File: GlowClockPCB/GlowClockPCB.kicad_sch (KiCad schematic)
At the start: 32 parts, among them J1 LED_OUT_1, J2 LED_OUT_2, J3 LED_OUT_3, J4 LED_OUT_4, J5 POWER_IN, U1 RaspberryPi_Pico_W, U2 Raspberry_Pi_Zero_2_W, U3 DS3231MZ

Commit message: add output connectors for motor drivers
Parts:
- added J6: Motor_1_Out, Connector_JST:JST_XH_B4B-XH-A_1x04_P2.50mm_Vertical, symbol Connector:Conn_01x04_Socket
- added J7: Motor_2_Out, Connector_JST:JST_XH_B4B-XH-A_1x04_P2.50mm_Vertical, symbol Connector:Conn_01x04_Socket
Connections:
- net at A1.3 (A2): now also J6.4 (Pin_4)
- net at A1.4 (A1): now also J6.3 (Pin_3)
- net at A1.5 (B1): now also J6.2 (Pin_2)
- net at A1.6 (B2): now also J6.1 (Pin_1)
- net at A2.3 (A2): now also J7.4 (Pin_4)
- net at A2.4 (A1): now also J7.3 (Pin_3)
- net at A2.5 (B1): now also J7.2 (Pin_2)
- net at A2.6 (B2): now also J7.1 (Pin_1)

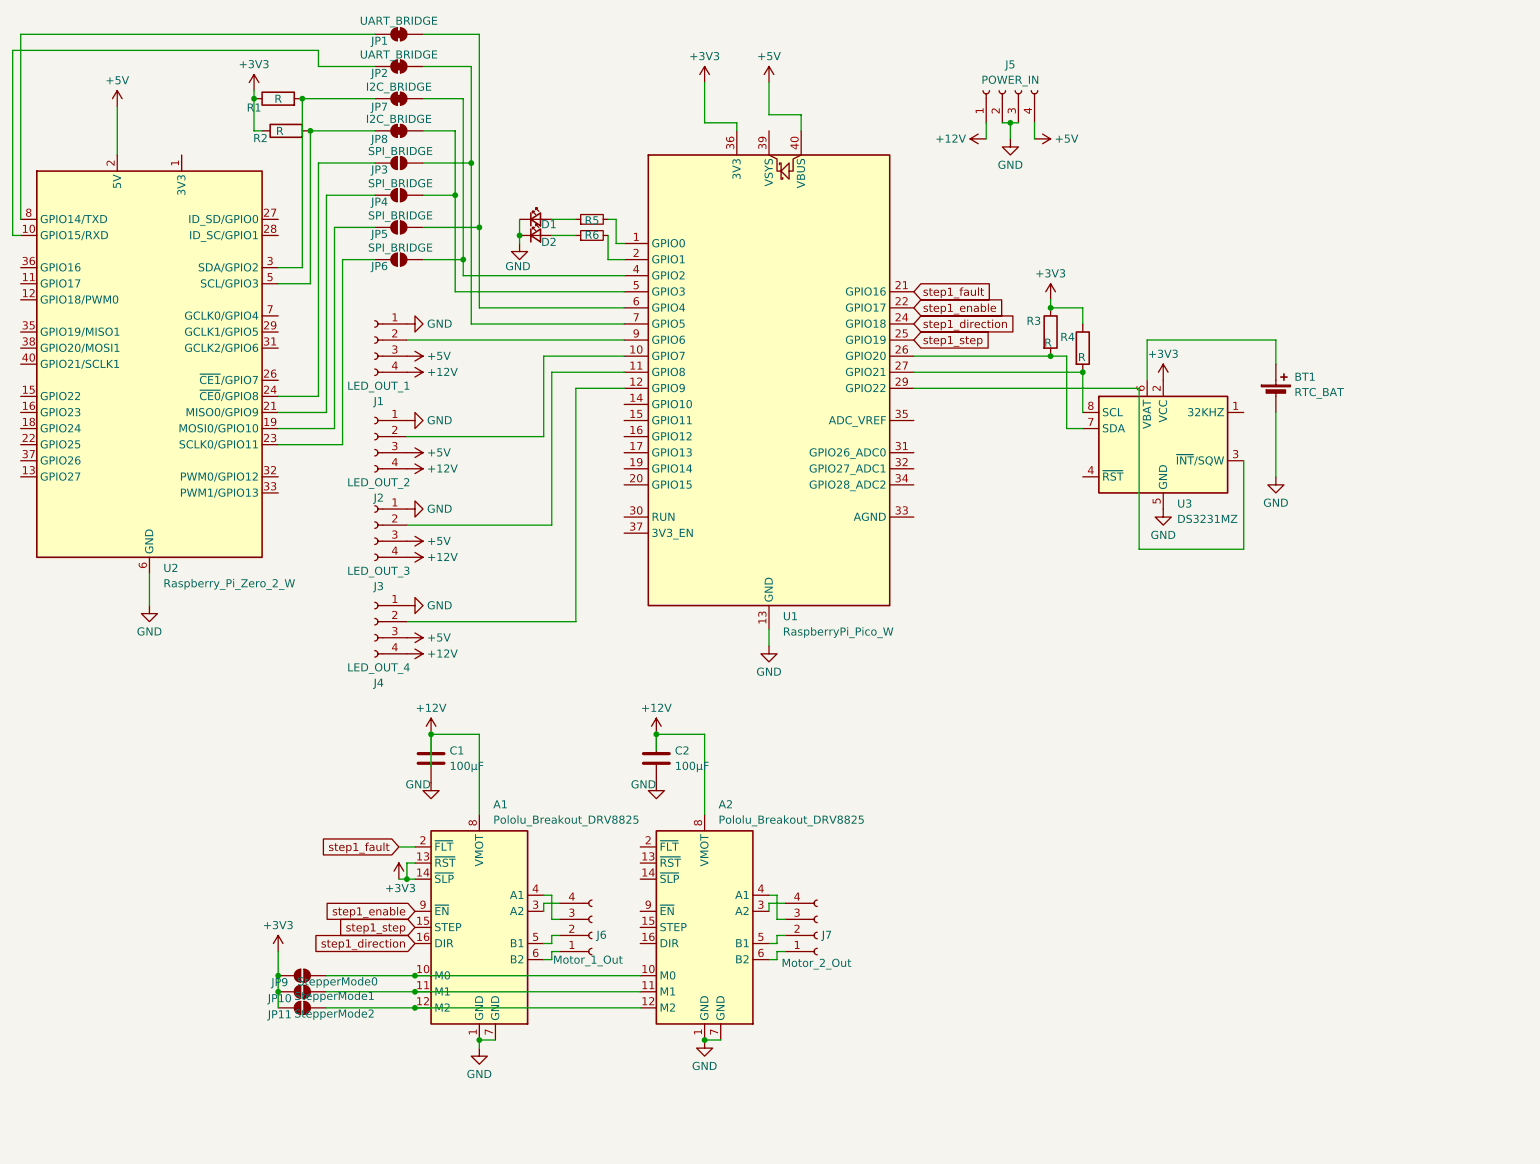
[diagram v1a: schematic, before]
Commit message: lots of tweaks to design, add display port, mounting holes, decoupling caps, etc
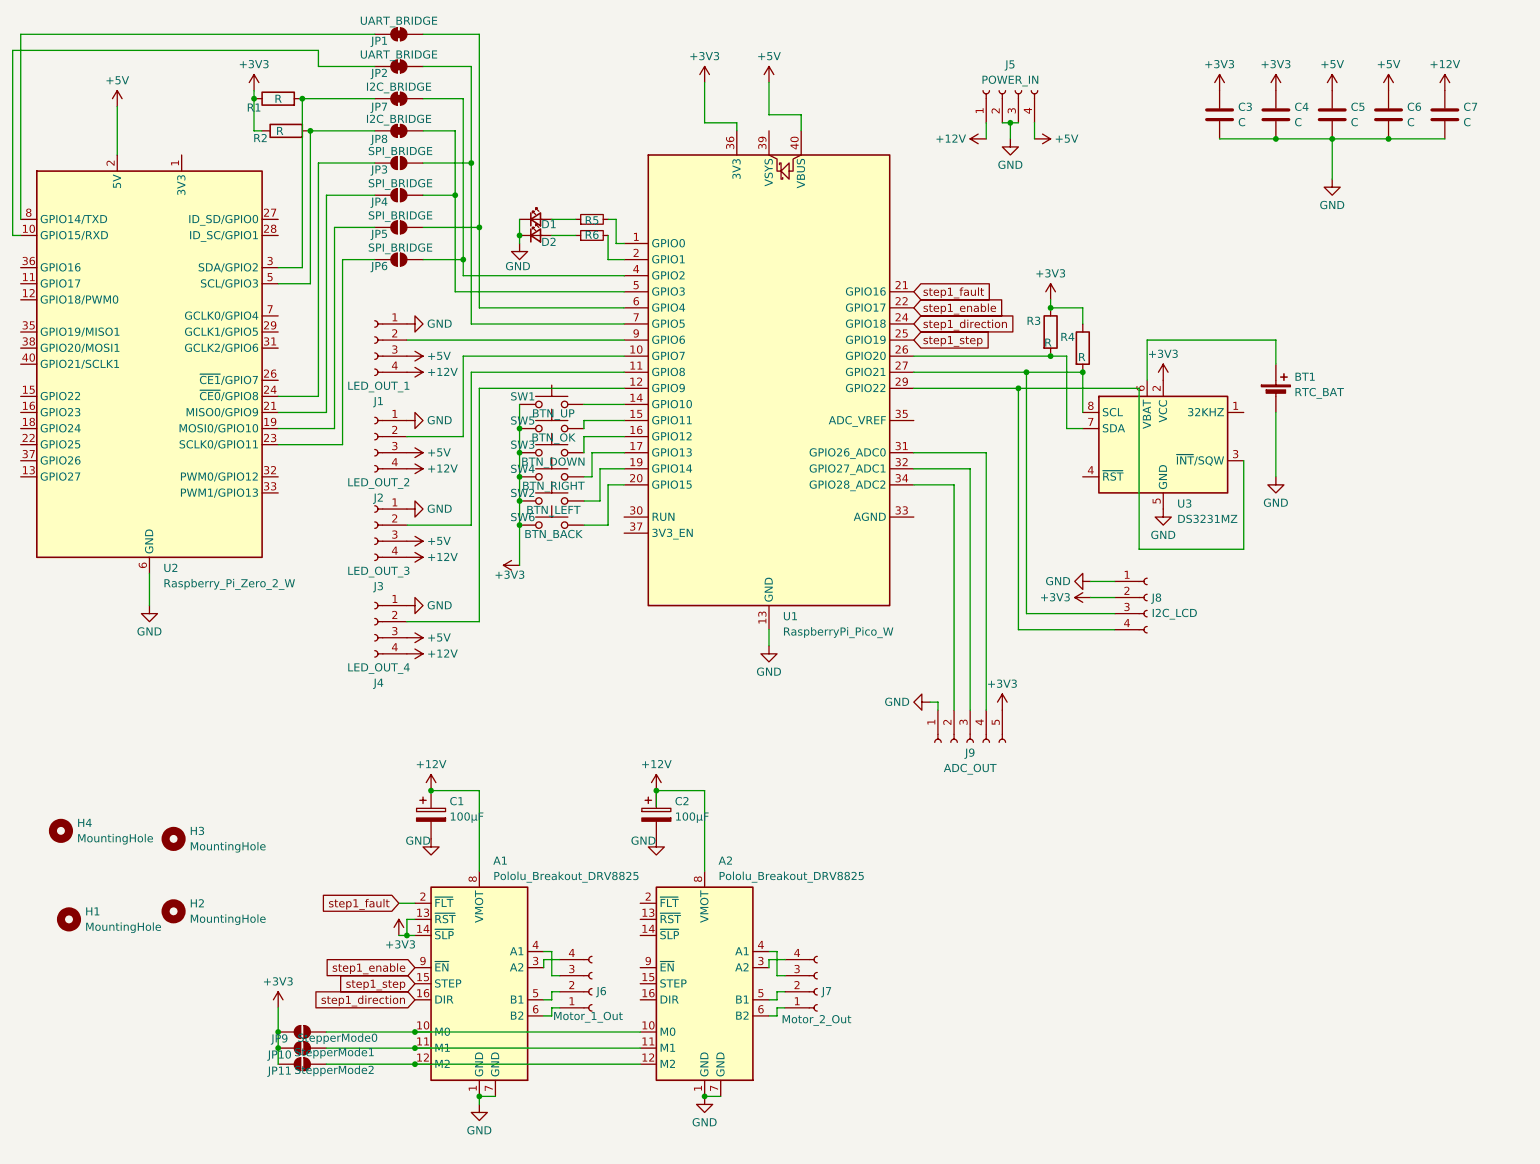
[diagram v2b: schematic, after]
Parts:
- added C3, C4, C5, C6, C7: C, Capacitor_SMD:C_0603_1608Metric, symbol Device:C
- added H1, H2, H3, H4: MountingHole, MountingHole:MountingHole_3.2mm_M3, symbol Mechanical:MountingHole
- added J8: I2C_LCD, Connector_PinHeader_2.54mm:PinHeader_1x04_P2.54mm_Vertical, symbol Connector:Conn_01x04_Socket
- added J9: ADC_OUT, Connector_JST:JST_XH_B5B-XH-A_1x05_P2.50mm_Vertical, symbol Connector:Conn_01x05_Socket
- added SW1: BTN_UP, Button_Switch_SMD:SW_Push_1P1T_NO_6x6mm_H9.5mm, symbol Switch:SW_Push
- added SW2: BTN_LEFT, Button_Switch_SMD:SW_Push_1P1T_NO_6x6mm_H9.5mm, symbol Switch:SW_Push
- added SW3: BTN_DOWN, Button_Switch_SMD:SW_Push_1P1T_NO_6x6mm_H9.5mm, symbol Switch:SW_Push
- added SW4: BTN_RIGHT, Button_Switch_SMD:SW_Push_1P1T_NO_6x6mm_H9.5mm, symbol Switch:SW_Push
- added SW5: BTN_OK, Button_Switch_SMD:SW_Push_1P1T_NO_6x6mm_H9.5mm, symbol Switch:SW_Push
- added SW6: BTN_BACK, Button_Switch_SMD:SW_Push_1P1T_NO_6x6mm_H9.5mm, symbol Switch:SW_Push
- C1, C2: footprint (none) -> Capacitor_THT:CP_Radial_D10.0mm_P5.00mm; symbol Device:C -> Device:C_Polarized
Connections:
- net +12V: now also C7.1
- net +3V3: now also C3.1, C4.1, J8.2 (Pin_2), J9.5 (Pin_5), SW1.1, SW2.1, SW3.1, SW4.1, SW5.1, SW6.1
- net +5V: now also C5.1, C6.1
- net GND: now also C3.2, C4.2, C5.2, C6.2, C7.2, J8.1 (Pin_1), J9.1 (Pin_1)
- net at R4.2, U1.27 (GPIO21), U3.8 (SCL): now also J8.3 (Pin_3)
- net at U1.14 (GPIO10): now also SW1.2
- net at U1.15 (GPIO11): now also SW5.2
- net at U1.16 (GPIO12): now also SW3.2
- net at U1.17 (GPIO13): now also SW4.2
- net at U1.19 (GPIO14): now also SW2.2
- net at U1.20 (GPIO15): now also SW6.2
- net at U1.29 (GPIO22), U3.3 (~{INT}/SQW): now also J8.4 (Pin_4)
- net at U1.31 (GPIO26_ADC0): now also J9.4 (Pin_4)
- net at U1.32 (GPIO27_ADC1): now also J9.3 (Pin_3)
- net at U1.34 (GPIO28_ADC2): now also J9.2 (Pin_2)
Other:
- moved on the sheet: A1, A2, J6, J7, JP10, JP11, JP9

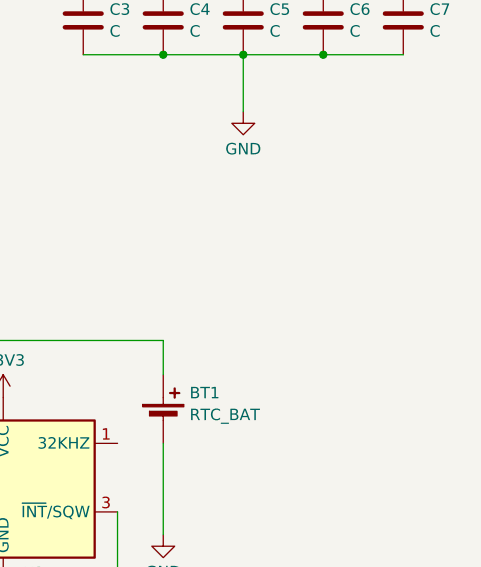
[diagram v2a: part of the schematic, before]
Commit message: tweaks to resolve DRC errors
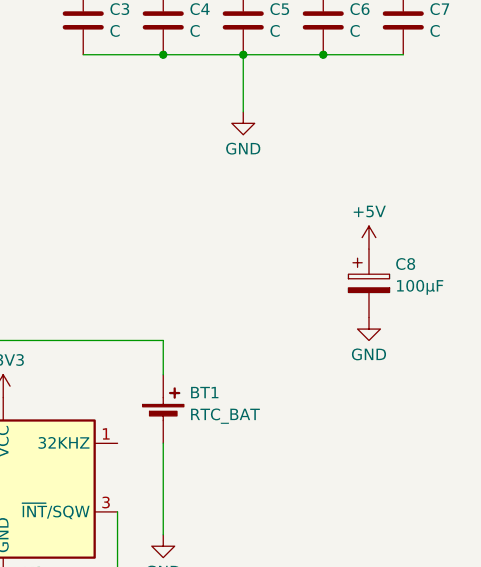
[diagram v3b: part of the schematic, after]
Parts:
- added C8: 100µF, Capacitor_THT:CP_Radial_D10.0mm_P5.00mm, symbol Device:C_Polarized
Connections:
- net +5V: now also C8.1
- net GND: now also C8.2
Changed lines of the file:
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@@
+	)
+	(symbol
+		(lib_id "Device:C_Polarized")
+		(at 255.27 63.5 0)
+		(unit 1)
+		(exclude_from_sim no)
+		(in_bom yes)
+		(on_board yes)
+		(dnp no)
+		(fields_autoplaced yes)
+		(property "Reference" "C8"
+			(at 258.191 61.3988 0)
+			(effects
+				(font
+					(size 1.27 1.27)
+				)
+				(justify left)
+			)
+		)
+		(property "Value" "100µF"
+			(at 258.191 63.8231 0)
+			(effects
+				(font
+					(size 1.27 1.27)
+				)
+				(justify left)
+			)
+		)
+		(property "Footprint" "Capacitor_THT:CP_Radial_D10.0mm_P5.00mm"
+			(at 256.2352 67.31 0)
+			(effects
+				(font
+					(size 1.27 1.27)
+				)
+				(hide yes)
+			)
+		)
+		(property "Datasheet" "~"
+			(at 255.27 63.5 0)
+			(effects
+				(font
+					(size 1.27 1.27)
+				)
+				(hide yes)
+			)
+		)
+		(property "Description" "Polarized capacitor"
+			(at 255.27 63.5 0)
+			(effects
+				(font
+					(size 1.27 1.27)
+				)
+				(hide yes)
+			)
+		)
+		(pin "1"
+		)
+		(pin "2"
+		)
+		(instances
+			(project "GlowClockPCB"
+				(path "/90c5669f-8ddc-43d0-a8ba-bdcfa424cd04"
+					(reference "C8")
+					(unit 1)
+				)
+			)
+		)
 	)
 	(symbol
@@
 	)
 	(symbol
+		(lib_id "power:GND")
+		(at 255.27 67.31 0)
+		(unit 1)
+		(exclude_from_sim no)
+		(in_bom yes)
+		(on_board yes)
+		(dnp no)
+		(fields_autoplaced yes)
+		(property "Reference" "#PWR047"
+			(at 255.27 73.66 0)
+			(effects
+				(font
+					(size 1.27 1.27)
+				)
+				(hide yes)
+			)
+		)
+		(property "Value" "GND"
+			(at 255.27 71.4431 0)
+			(effects
+				(font
+					(size 1.27 1.27)
+				)
+			)
+		)
+		(property "Footprint" ""
+			(at 255.27 67.31 0)
+			(effects
+				(font
+					(size 1.27 1.27)
+				)
+				(hide yes)
+			)
+		)
+		(property "Datasheet" ""
+			(at 255.27 67.31 0)
+			(effects
+				(font
+					(size 1.27 1.27)
+				)
+				(hide yes)
+			)
+		)
+		(property "Description" "Power symbol creates a global label with name \"GND\" , ground"
+			(at 255.27 67.31 0)
+			(effects
+				(font
+					(size 1.27 1.27)
+				)
+				(hide yes)
+			)
+		)
+		(pin "1"
+		)
+		(instances
+			(project ""
+				(path "/90c5669f-8ddc-43d0-a8ba-bdcfa424cd04"
+					(reference "#PWR047")
+					(unit 1)
+				)
+			)
+		)
+	)
+	(symbol
 		(lib_id "power:+3V3")
 		(at 189.23 128.27 0)
@@
 					(unit 1)
 				)
+			)
+		)
+	)
+	(symbol
+		(lib_id "power:+5V")
+		(at 255.27 59.69 0)
+		(unit 1)
+		(exclude_from_sim no)
+		(in_bom yes)
+		(on_board yes)
+		(dnp no)
+		(fields_autoplaced yes)
+		(property "Reference" "#PWR046"
+			(at 255.27 63.5 0)
+			(effects
+				(font
+					(size 1.27 1.27)
+				)
+				(hide yes)
+			)
+		)
+		(property "Value" "+5V"
+			(at 255.27 55.5569 0)
+			(effects
+				(font
+					(size 1.27 1.27)
+				)
+			)
+		)
+		(property "Footprint" ""
+			(at 255.27 59.69 0)
+			(effects
+				(font
+					(size 1.27 1.27)
+				)
+				(hide yes)
+			)
+		)
+		(property "Datasheet" ""
+			(at 255.27 59.69 0)
+			(effects
+				(font
+					(size 1.27 1.27)
+				)
+				(hide yes)
+			)
+		)
+		(property "Description" "Power symbol creates a global label with name \"+5V\""
+			(at 255.27 59.69 0)
+			(effects
+				(font
+					(size 1.27 1.27)
+				)
+				(hide yes)
+			)
+		)
+		(pin "1"
+		)
+		(instances
+			(project ""
+				(path "/90c5669f-8ddc-43d0-a8ba-bdcfa424cd04"
+					(reference "#PWR046")
+					(unit 1)
+				)

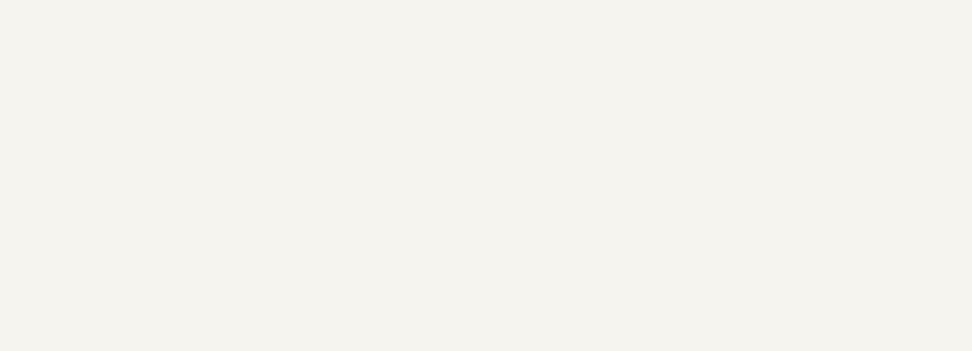
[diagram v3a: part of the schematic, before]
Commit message: finalize design for export, add schematic to docs
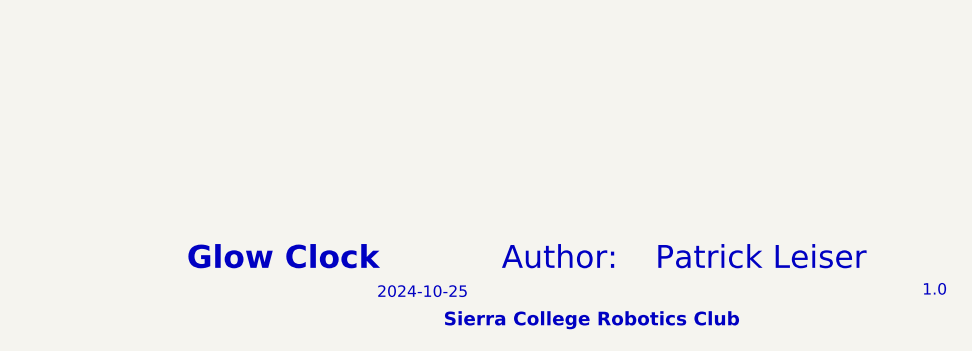
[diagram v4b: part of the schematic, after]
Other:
- note added: "1.0"
- note added: "2024-10-25"
- note added: "Author:"
- note added: "Glow Clock"
- note added: "Patrick Leiser"
- note added: "Sierra College Robotics Club"
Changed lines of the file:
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@@
+		)
+	)
+	(text "1.0"
+		(exclude_from_sim no)
+		(at 270.002 193.294 0)
+		(effects
+			(font
+				(size 1.27 1.27)
+			)
+		)
+	)
+	(text "Glow Clock"
+		(exclude_from_sim no)
+		(at 197.612 189.738 0)
+		(effects
+			(font
+				(size 2.54 2.54)
+				(thickness 0.508)
+				(bold yes)
+			)
+		)
+	)
+	(text "Author: "
+		(exclude_from_sim no)
+		(at 228.346 189.738 0)
+		(effects
+			(font
+				(size 2.54 2.54)
+				(color 132 0 0 1)
+			)
+		)
+	)
+	(text "Patrick Leiser"
+		(exclude_from_sim no)
+		(at 250.698 189.738 0)
+		(effects
+			(font
+				(size 2.54 2.54)
+			)
+		)
+	)
+	(text "Sierra College Robotics Club"
+		(exclude_from_sim no)
+		(at 231.902 196.596 0)
+		(effects
+			(font
+				(size 1.5 1.5)
+				(thickness 0.254)
+				(bold yes)
+			)
+		)
+	)
+	(text "2024-10-25"
+		(exclude_from_sim no)
+		(at 213.106 193.548 0)
+		(effects
+			(font
+				(size 1.27 1.27)
+			)
 		)
 	)
